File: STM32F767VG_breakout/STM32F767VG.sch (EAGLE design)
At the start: 42 parts, among them IC1 STM32F767VGT6, IC3 LD117AS33TR, X4 8MHz, X5 32.768kHz

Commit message: Incorporated April 6 Comments
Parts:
- removed U$1: -L7805, tango:-L7805
- added IC2: L7805CV, L7805CV:L7805CV
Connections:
- net 12V: now also IC2.INPUT; no longer U$1.IN
- net 5V: now also IC2.OUTPUT; no longer U$1.OUT
- net GND: now also IC2.GROUND; no longer U$1.GND
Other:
- moved on the sheet: BEAD4, BT2, C16
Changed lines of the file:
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@@
 <part name="C1" library="eagle-ltspice" library_urn="urn:adsk.eagle:library:217" deviceset="C" device="" package3d_urn="urn:adsk.eagle:package:13265/1" value="100nF"/>
 <part name="BT2" library="pinhead" library_urn="urn:adsk.eagle:library:325" deviceset="PINHD-1X2" device="" package3d_urn="urn:adsk.eagle:package:22435/2"/>
-<part name="U$1" library="tango" deviceset="-L7805" device=""/>
+<part name="IC2" library="L7805CV" deviceset="L7805CV" device=""/>
 </parts>
 <sheets>
@@
 <instance part="IC3" gate="G$1" x="152.4" y="22.86"/>
 <instance part="SUPPLY15" gate="VDD" x="167.64" y="22.86" rot="R270"/>
-<instance part="BEAD4" gate="G$1" x="119.38" y="7.62" rot="R90"/>
-<instance part="C16" gate="G$1" x="116.84" y="30.48"/>
+<instance part="BEAD4" gate="G$1" x="104.14" y="7.62" rot="R90"/>
+<instance part="C16" gate="G$1" x="101.6" y="30.48"/>
 <instance part="C17" gate="G$1" x="139.7" y="33.02"/>
 <instance part="R6" gate="G$1" x="162.56" y="35.56" rot="R90"/>
@@
 <instance part="GND4" gate="1" x="-12.7" y="40.64" rot="R90"/>
 <instance part="C1" gate="G$1" x="-20.32" y="-78.74"/>
-<instance part="BT2" gate="G$1" x="101.6" y="20.32" rot="MR0"/>
-<instance part="U$1" gate="G$1" x="129.54" y="22.86"/>
+<instance part="BT2" gate="G$1" x="86.36" y="20.32" rot="MR0"/>
+<instance part="IC2" gate="G$1" x="104.14" y="22.86"/>
 </instances>
 <busses>
@@
 <pinref part="BEAD4" gate="G$1" pin="2"/>
 <pinref part="IC3" gate="G$1" pin="ADJ"/>
-<wire x1="124.46" y1="7.62" x2="129.54" y2="7.62" width="0.1524" layer="91"/>
-<wire x1="129.54" y1="7.62" x2="152.4" y2="7.62" width="0.1524" layer="91"/>
+<wire x1="109.22" y1="7.62" x2="124.46" y2="7.62" width="0.1524" layer="91"/>
+<wire x1="124.46" y1="7.62" x2="152.4" y2="7.62" width="0.1524" layer="91"/>
 <wire x1="152.4" y1="7.62" x2="152.4" y2="15.24" width="0.1524" layer="91"/>
-<wire x1="129.54" y1="17.78" x2="129.54" y2="7.62" width="0.1524" layer="91"/>
-<junction x="129.54" y="7.62"/>
 <label x="139.7" y="7.62" size="1.778" layer="95"/>
-<pinref part="U$1" gate="G$1" pin="GND"/>
+<pinref part="IC2" gate="G$1" pin="GROUND"/>
+<wire x1="104.14" y1="20.32" x2="104.14" y2="12.7" width="0.1524" layer="91"/>
+<wire x1="104.14" y1="12.7" x2="124.46" y2="12.7" width="0.1524" layer="91"/>
+<wire x1="124.46" y1="12.7" x2="124.46" y2="7.62" width="0.1524" layer="91"/>
+<junction x="124.46" y="7.62"/>
 </segment>
 <segment>
@@
 <net name="12V" class="0">
 <segment>
-<label x="114.3" y="20.32" size="1.778" layer="95"/>
+<label x="99.06" y="20.32" size="1.778" layer="95"/>
 <pinref part="C16" gate="G$1" pin="2"/>
-<wire x1="116.84" y1="25.4" x2="116.84" y2="22.86" width="0.1524" layer="91"/>
+<wire x1="101.6" y1="25.4" x2="101.6" y2="22.86" width="0.1524" layer="91"/>
 <pinref part="BT2" gate="G$1" pin="1"/>
-<wire x1="104.14" y1="22.86" x2="116.84" y2="22.86" width="0.1524" layer="91"/>
-<pinref part="U$1" gate="G$1" pin="IN"/>
-<wire x1="121.92" y1="25.4" x2="121.92" y2="22.86" width="0.1524" layer="91"/>
-<wire x1="121.92" y1="22.86" x2="116.84" y2="22.86" width="0.1524" layer="91"/>
-<junction x="116.84" y="22.86"/>
+<wire x1="88.9" y1="22.86" x2="101.6" y2="22.86" width="0.1524" layer="91"/>
+<pinref part="IC2" gate="G$1" pin="INPUT"/>
+<wire x1="104.14" y1="22.86" x2="101.6" y2="22.86" width="0.1524" layer="91"/>
+<junction x="101.6" y="22.86"/>
 </segment>
 <segment>
@@
 <label x="139.7" y="20.32" size="1.778" layer="95"/>
 <wire x1="139.7" y1="22.86" x2="144.78" y2="22.86" width="0.1524" layer="91"/>
-<wire x1="139.7" y1="27.94" x2="139.7" y2="25.4" width="0.1524" layer="91"/>
 <pinref part="C17" gate="G$1" pin="2"/>
-<pinref part="U$1" gate="G$1" pin="OUT"/>
-<wire x1="139.7" y1="25.4" x2="139.7" y2="22.86" width="0.1524" layer="91"/>
-<wire x1="137.16" y1="25.4" x2="139.7" y2="25.4" width="0.1524" layer="91"/>
-<junction x="139.7" y="25.4"/>
+<wire x1="139.7" y1="27.94" x2="139.7" y2="22.86" width="0.1524" layer="91"/>
+<pinref part="IC2" gate="G$1" pin="OUTPUT"/>
+<wire x1="137.16" y1="22.86" x2="139.7" y2="22.86" width="0.1524" layer="91"/>
+<junction x="139.7" y="22.86"/>
 </segment>
 </net>
@@
 <segment>
 <pinref part="BEAD4" gate="G$1" pin="1"/>
-<wire x1="114.3" y1="17.78" x2="114.3" y2="7.62" width="0.1524" layer="91"/>
-<label x="114.3" y="10.16" size="1.778" layer="95" rot="R90"/>
+<wire x1="99.06" y1="17.78" x2="99.06" y2="7.62" width="0.1524" layer="91"/>
+<label x="99.06" y="10.16" size="1.778" layer="95" rot="R90"/>
 <pinref part="BT2" gate="G$1" pin="2"/>
-<wire x1="114.3" y1="17.78" x2="104.14" y2="17.78" width="0.1524" layer="91"/>
-<wire x1="104.14" y1="17.78" x2="104.14" y2="20.32" width="0.1524" layer="91"/>
+<wire x1="99.06" y1="17.78" x2="88.9" y2="17.78" width="0.1524" layer="91"/>
+<wire x1="88.9" y1="17.78" x2="88.9" y2="20.32" width="0.1524" layer="91"/>
 </segment>
 <segment>
 <pinref part="C16" gate="G$1" pin="1"/>
-<wire x1="116.84" y1="33.02" x2="116.84" y2="45.72" width="0.1524" layer="91"/>
-<label x="116.84" y="38.1" size="1.778" layer="95" rot="R90"/>
-</segment>
-</net>
+<wire x1="101.6" y1="33.02" x2="101.6" y2="45.72" width="0.1524" layer="91"/>
+<label x="101.6" y="38.1" size="1.778" layer="95" rot="R90"/>
+</segment>
+</net>

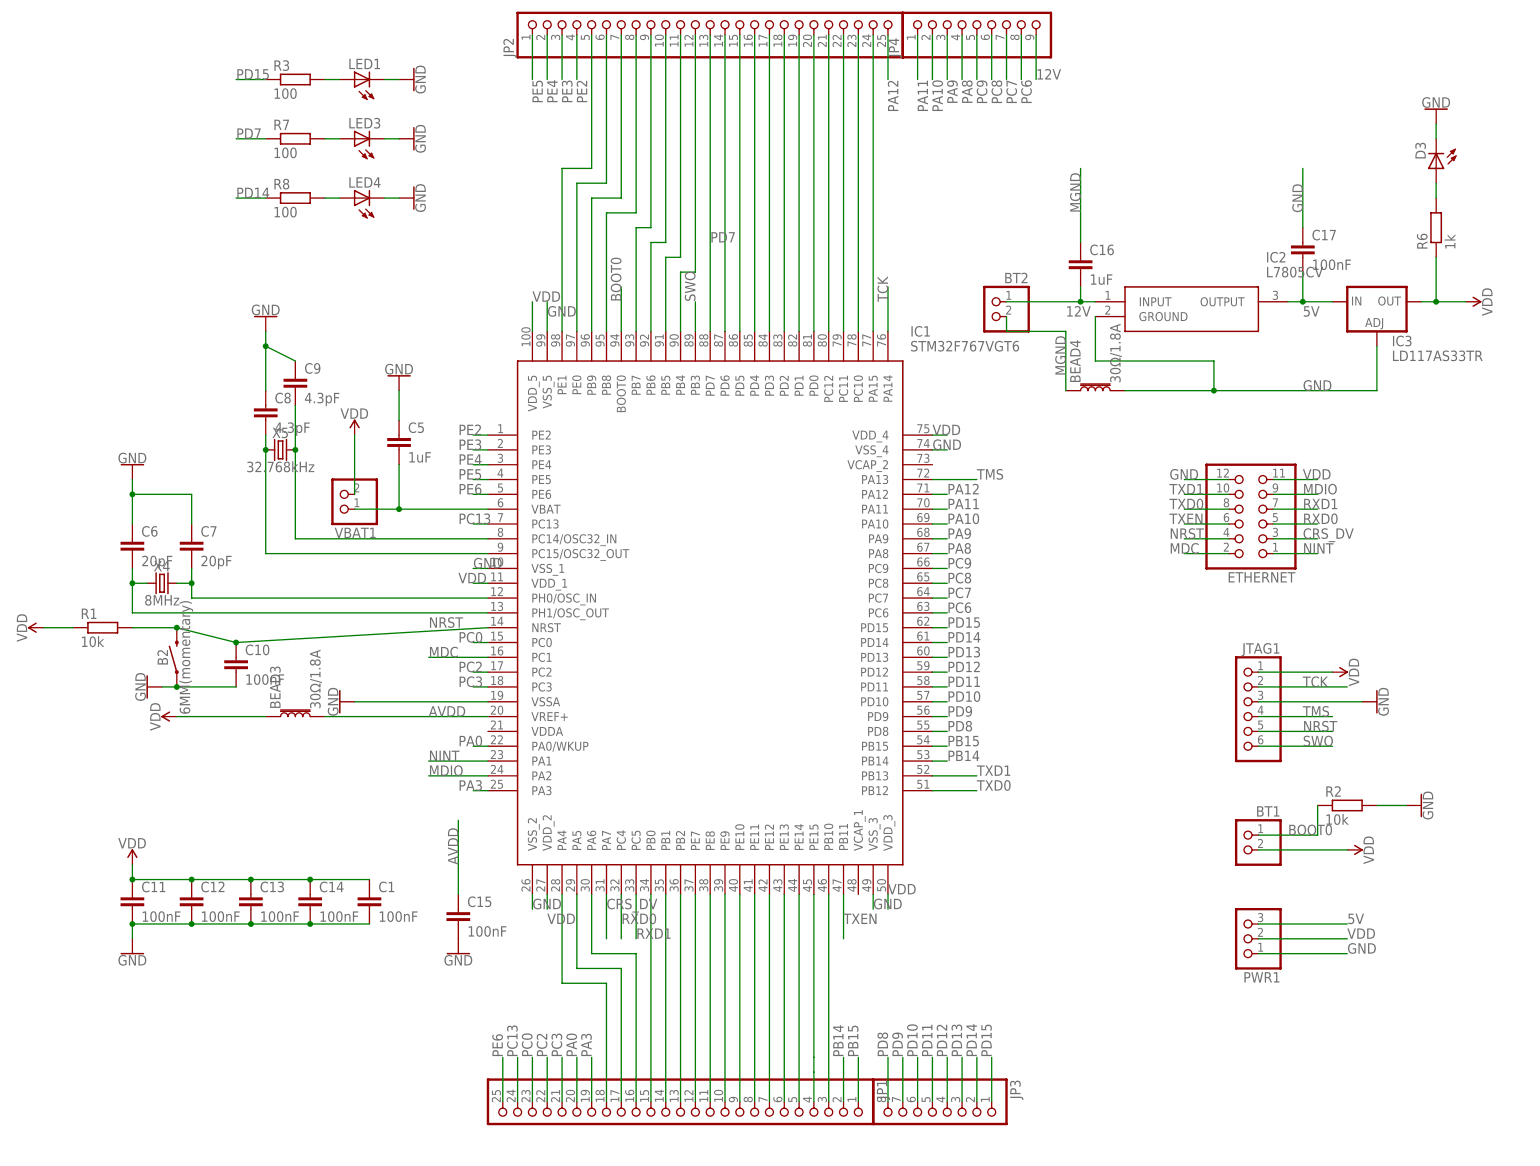
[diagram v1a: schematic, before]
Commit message: Current routing progress
Routed most of top breakout pins
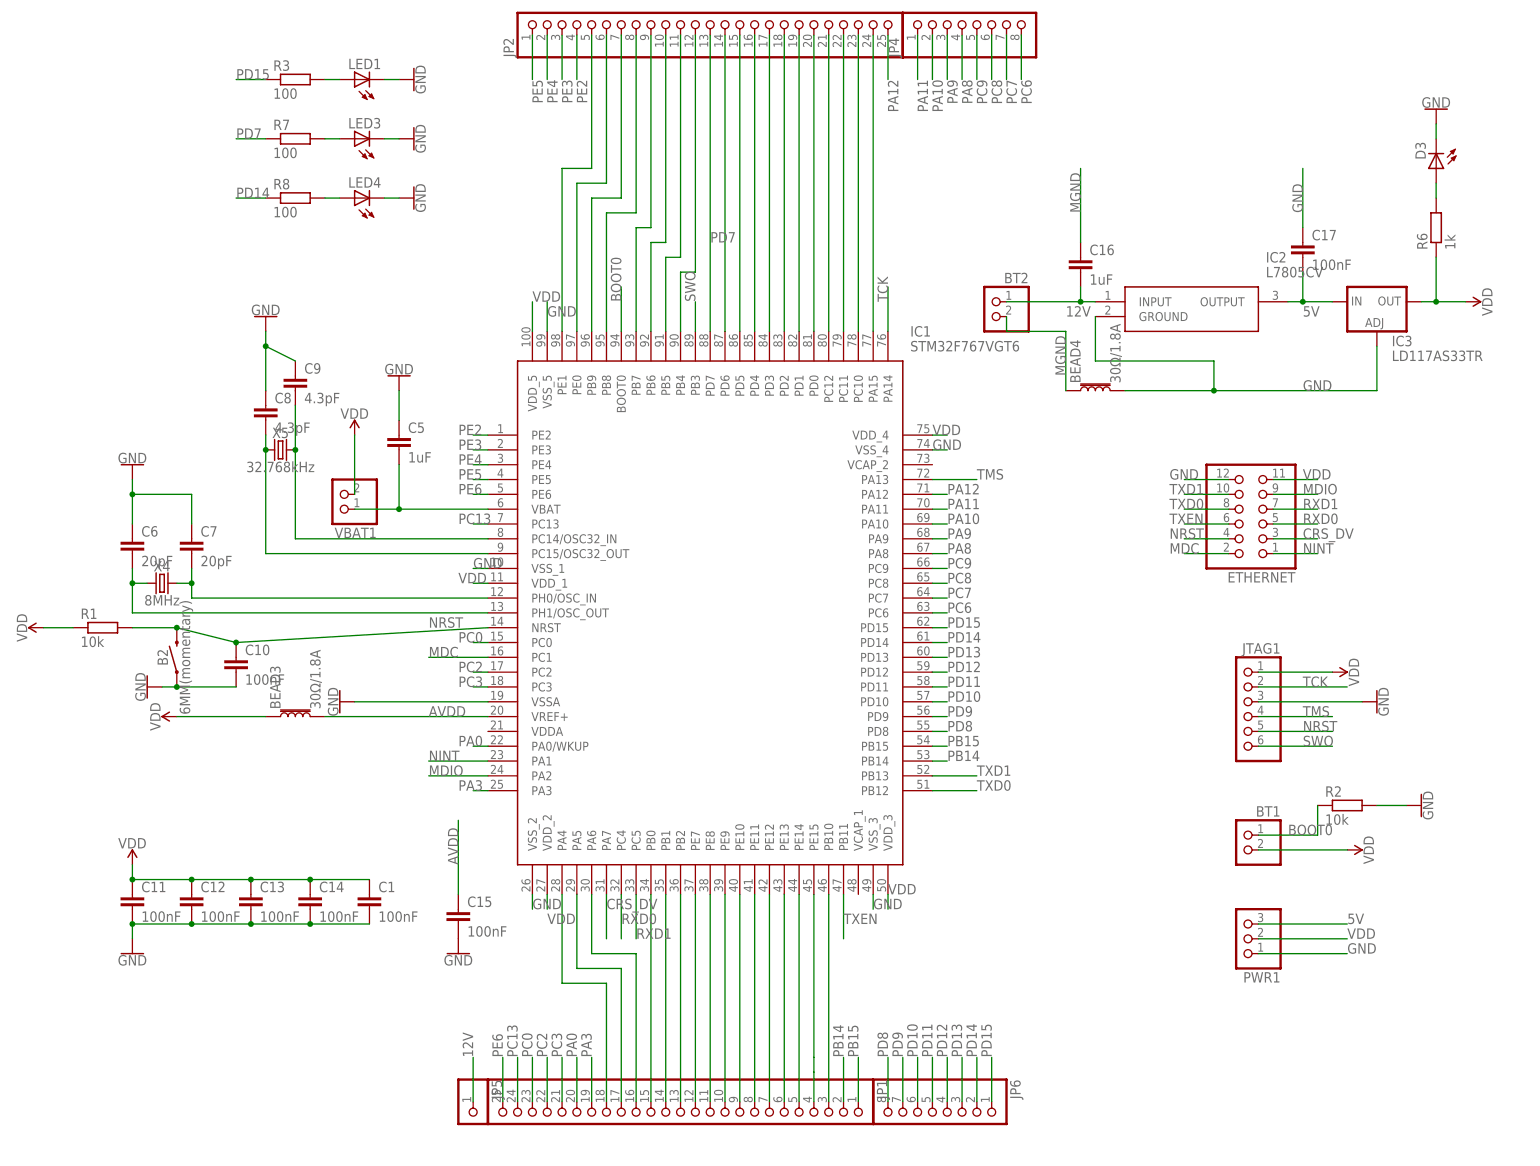
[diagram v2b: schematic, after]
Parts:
- added JP5: (no value), pinhead:PINHD-1X1
- JP4: device pinhead:PINHD-1X9 -> pinhead:PINHD-1X8
- renumbered JP3 to JP6
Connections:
- net 12V: now also JP5.1; no longer JP4.9
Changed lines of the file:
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@@
 <part name="JP1" library="pinhead" library_urn="urn:adsk.eagle:library:325" deviceset="PINHD-1X25" device="" package3d_urn="urn:adsk.eagle:package:22473/1"/>
 <part name="JP2" library="pinhead" library_urn="urn:adsk.eagle:library:325" deviceset="PINHD-1X25" device="" package3d_urn="urn:adsk.eagle:package:22473/1"/>
-<part name="JP3" library="pinhead" library_urn="urn:adsk.eagle:library:325" deviceset="PINHD-1X8" device="" package3d_urn="urn:adsk.eagle:package:22409/2"/>
-<part name="JP4" library="pinhead" library_urn="urn:adsk.eagle:library:325" deviceset="PINHD-1X9" device="" package3d_urn="urn:adsk.eagle:package:22483/1"/>
+<part name="JP4" library="pinhead" library_urn="urn:adsk.eagle:library:325" deviceset="PINHD-1X8" device="" package3d_urn="urn:adsk.eagle:package:22409/2"/>
 <part name="SUPPLY1" library="SparkFun-PowerSymbols" deviceset="VDD" device=""/>
 <part name="R1" library="eagle-ltspice" library_urn="urn:adsk.eagle:library:217" deviceset="R" device="" package3d_urn="urn:adsk.eagle:package:13300/1" value="10k"/>
@@
 <part name="BT2" library="pinhead" library_urn="urn:adsk.eagle:library:325" deviceset="PINHD-1X2" device="" package3d_urn="urn:adsk.eagle:package:22435/2"/>
 <part name="IC2" library="L7805CV" deviceset="L7805CV" device=""/>
+<part name="JP5" library="pinhead" library_urn="urn:adsk.eagle:library:325" deviceset="PINHD-1X1" device="" package3d_urn="urn:adsk.eagle:package:22485/1"/>
+<part name="JP6" library="pinhead" library_urn="urn:adsk.eagle:library:325" deviceset="PINHD-1X8" device="" package3d_urn="urn:adsk.eagle:package:22409/2"/>
 </parts>
 <sheets>
@@
 <instance part="JP1" gate="A" x="33.02" y="-116.84" rot="R270"/>
 <instance part="JP2" gate="A" x="38.1" y="71.12" rot="R90"/>
-<instance part="JP3" gate="A" x="76.2" y="-116.84" rot="R270"/>
 <instance part="JP4" gate="A" x="83.82" y="71.12" rot="R90"/>
 <instance part="SUPPLY1" gate="VDD" x="-76.2" y="-33.02" rot="R90"/>
@@
 <instance part="BT2" gate="G$1" x="86.36" y="20.32" rot="MR0"/>
 <instance part="IC2" gate="G$1" x="104.14" y="22.86"/>
+<instance part="JP5" gate="G$1" x="-2.54" y="-116.84" rot="R270"/>
+<instance part="JP6" gate="A" x="76.2" y="-116.84" rot="R270"/>
 </instances>
 <busses>
@@
 </segment>
 <segment>
-<pinref part="JP4" gate="A" pin="9"/>
-<wire x1="93.98" y1="68.58" x2="93.98" y2="60.96" width="0.1524" layer="91"/>
-<label x="93.98" y="60.96" size="1.778" layer="95"/>
+<pinref part="JP5" gate="G$1" pin="1"/>
+<wire x1="-2.54" y1="-114.3" x2="-2.54" y2="-106.68" width="0.1524" layer="91"/>
+<label x="-2.54" y="-106.68" size="1.778" layer="95" rot="R90"/>
 </segment>
 </net>
@@
 </segment>
 <segment>
-<pinref part="JP3" gate="A" pin="8"/>
-<wire x1="68.58" y1="-114.3" x2="68.58" y2="-106.68" width="0.1524" layer="91"/>
 <label x="68.58" y="-106.68" size="1.778" layer="95" rot="R90"/>
+<pinref part="JP6" gate="A" pin="8"/>
+<wire x1="68.58" y1="-106.68" x2="68.58" y2="-114.3" width="0.1524" layer="91"/>
 </segment>
 </net>
@@
 </segment>
 <segment>
-<pinref part="JP3" gate="A" pin="7"/>
-<wire x1="71.12" y1="-106.68" x2="71.12" y2="-114.3" width="0.1524" layer="91"/>
 <label x="71.12" y="-106.68" size="1.778" layer="95" rot="R90"/>
+<pinref part="JP6" gate="A" pin="7"/>
+<wire x1="71.12" y1="-114.3" x2="71.12" y2="-106.68" width="0.1524" layer="91"/>
 </segment>
 </net>
@@
 </segment>
 <segment>
-<pinref part="JP3" gate="A" pin="6"/>
-<wire x1="73.66" y1="-114.3" x2="73.66" y2="-106.68" width="0.1524" layer="91"/>
 <label x="73.66" y="-106.68" size="1.778" layer="95" rot="R90"/>
+<pinref part="JP6" gate="A" pin="6"/>
+<wire x1="73.66" y1="-106.68" x2="73.66" y2="-114.3" width="0.1524" layer="91"/>
 </segment>
 </net>
@@
 </segment>
 <segment>
-<pinref part="JP3" gate="A" pin="5"/>
+<label x="76.2" y="-106.68" size="1.778" layer="95" rot="R90"/>
+<pinref part="JP6" gate="A" pin="5"/>
 <wire x1="76.2" y1="-106.68" x2="76.2" y2="-114.3" width="0.1524" layer="91"/>
-<label x="76.2" y="-106.68" size="1.778" layer="95" rot="R90"/>
 </segment>
 </net>
@@
 </segment>
 <segment>
-<pinref part="JP3" gate="A" pin="4"/>
+<label x="78.74" y="-106.68" size="1.778" layer="95" rot="R90"/>
+<pinref part="JP6" gate="A" pin="4"/>
 <wire x1="78.74" y1="-114.3" x2="78.74" y2="-106.68" width="0.1524" layer="91"/>
-<label x="78.74" y="-106.68" size="1.778" layer="95" rot="R90"/>
 </segment>
 </net>
@@
 </segment>
 <segment>
-<pinref part="JP3" gate="A" pin="3"/>
-<wire x1="81.28" y1="-114.3" x2="81.28" y2="-106.68" width="0.1524" layer="91"/>
 <label x="81.28" y="-106.68" size="1.778" layer="95" rot="R90"/>
+<pinref part="JP6" gate="A" pin="3"/>
+<wire x1="81.28" y1="-106.68" x2="81.28" y2="-114.3" width="0.1524" layer="91"/>
 </segment>
 </net>
@@
 </segment>
 <segment>
-<pinref part="JP3" gate="A" pin="2"/>
-<wire x1="83.82" y1="-114.3" x2="83.82" y2="-106.68" width="0.1524" layer="91"/>
 <label x="83.82" y="-106.68" size="1.778" layer="95" rot="R90"/>
+<pinref part="JP6" gate="A" pin="2"/>
+<wire x1="83.82" y1="-106.68" x2="83.82" y2="-114.3" width="0.1524" layer="91"/>
 </segment>
 <segment>
@@
 </segment>
 <segment>
-<pinref part="JP3" gate="A" pin="1"/>
+<label x="86.36" y="-106.68" size="1.778" layer="95" rot="R90"/>
+<pinref part="JP6" gate="A" pin="1"/>
 <wire x1="86.36" y1="-114.3" x2="86.36" y2="-106.68" width="0.1524" layer="91"/>
-<label x="86.36" y="-106.68" size="1.778" layer="95" rot="R90"/>
-</segment>
-<segment>
+</segment>
+<segment>
